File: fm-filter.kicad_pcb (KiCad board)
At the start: 2 copper layers, 57.2 x 29.2 mm, 7 parts, among them J1 SMA, J2 SMA

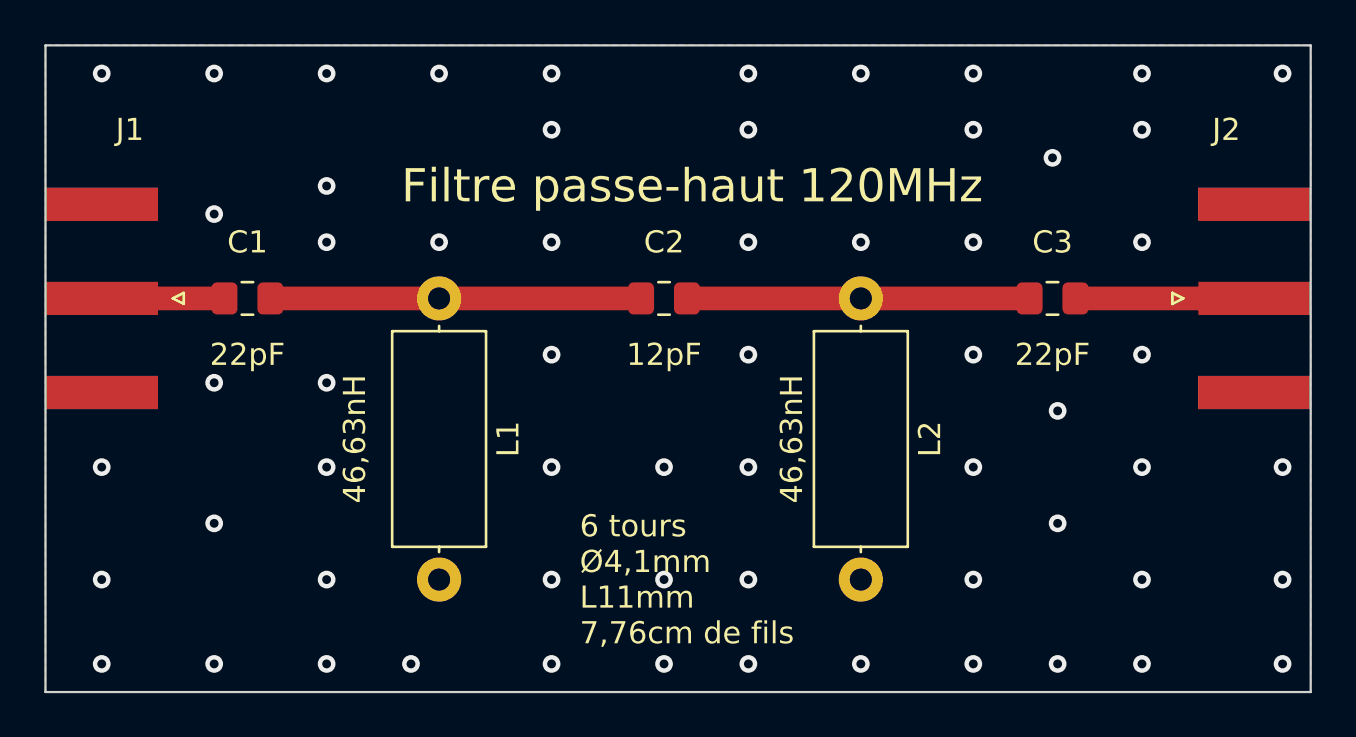
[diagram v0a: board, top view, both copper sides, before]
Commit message: feat: separative wall
Migrate to KiCAD v7.
Update README.md with initial manual and online order tentative.
Move to a newer version with mounting holes and pin holes for the wall
support.
Test integration with aisler.net
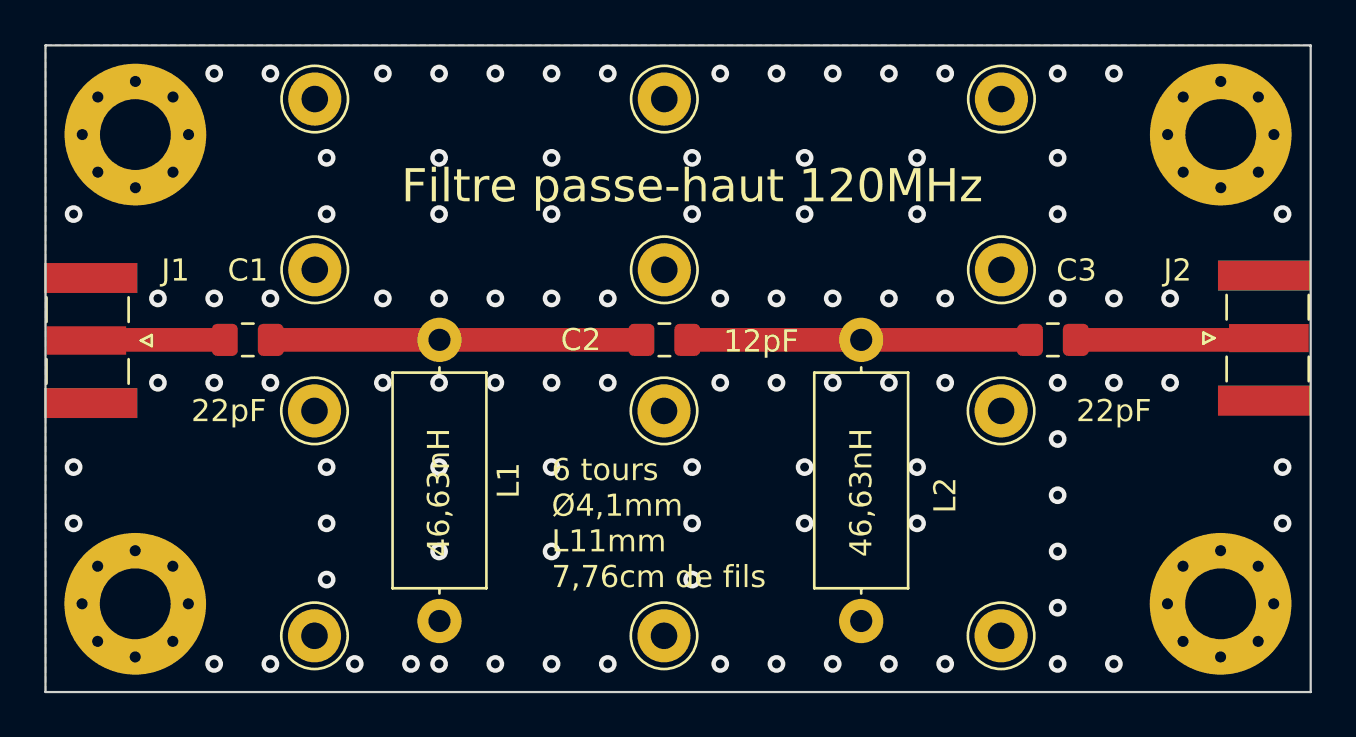
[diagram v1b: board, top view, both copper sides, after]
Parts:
- added MH1: Pin_D1.0mm_L10.0mm_LooseFit, Connector_Pin:Pin_D1.0mm_L10.0mm_LooseFit, F.Cu at (80.7, 34.2)
- added MH11: Pin_D1.0mm_L10.0mm_LooseFit, Connector_Pin:Pin_D1.0mm_L10.0mm_LooseFit, F.Cu at (96.5, 34.2)
- added MH12: Pin_D1.0mm_L10.0mm_LooseFit, Connector_Pin:Pin_D1.0mm_L10.0mm_LooseFit, F.Cu at (96.5, 41.9)
- added MH13: Pin_D1.0mm_L10.0mm_LooseFit, Connector_Pin:Pin_D1.0mm_L10.0mm_LooseFit, F.Cu at (96.5, 48.3)
- added MH14: Pin_D1.0mm_L10.0mm_LooseFit, Connector_Pin:Pin_D1.0mm_L10.0mm_LooseFit, F.Cu at (96.5, 58.4)
- added MH2: Pin_D1.0mm_L10.0mm_LooseFit, Connector_Pin:Pin_D1.0mm_L10.0mm_LooseFit, F.Cu at (80.7, 41.9)
- added MH21: Pin_D1.0mm_L10.0mm_LooseFit, Connector_Pin:Pin_D1.0mm_L10.0mm_LooseFit, F.Cu at (111.8, 34.2)
- added MH22: Pin_D1.0mm_L10.0mm_LooseFit, Connector_Pin:Pin_D1.0mm_L10.0mm_LooseFit, F.Cu at (111.8, 41.9)
- added MH23: Pin_D1.0mm_L10.0mm_LooseFit, Connector_Pin:Pin_D1.0mm_L10.0mm_LooseFit, F.Cu at (111.7, 48.3)
- added MH24: Pin_D1.0mm_L10.0mm_LooseFit, Connector_Pin:Pin_D1.0mm_L10.0mm_LooseFit, F.Cu at (111.7, 58.4)
- added MH3: Pin_D1.0mm_L10.0mm_LooseFit, Connector_Pin:Pin_D1.0mm_L10.0mm_LooseFit, F.Cu at (80.7, 48.3)
- added MH4: Pin_D1.0mm_L10.0mm_LooseFit, Connector_Pin:Pin_D1.0mm_L10.0mm_LooseFit, F.Cu at (80.7, 58.4)
- added MH_bottom_left: MountingHole_3.2mm_M3_Pad_Via, MountingHole:MountingHole_3.2mm_M3_Pad_Via, F.Cu at (72.6, 57.0)
- added MH_bottom_right: MountingHole_3.2mm_M3_Pad_Via, MountingHole:MountingHole_3.2mm_M3_Pad_Via, F.Cu at (121.7, 57.0)
- added MH_top_left: MountingHole_3.2mm_M3_Pad_Via, MountingHole:MountingHole_3.2mm_M3_Pad_Via, F.Cu at (72.6, 35.8)
- added MH_top_right: MountingHole_3.2mm_M3_Pad_Via, MountingHole:MountingHole_3.2mm_M3_Pad_Via, F.Cu at (121.7, 35.8)
- J1, J2: footprint Connector_Coaxial:SMA_Amphenol_132289_EdgeMount -> Connector_Coaxial:SMA_Samtec_SMA-J-P-X-ST-EM1_EdgeMount
- moved J1 1.97 mm to (70.6, 45.1), turned to -90 degrees
- moved C1 1.87 mm to (77.7, 45.1)
- moved C2 1.87 mm to (96.5, 45.1)
- moved C3 1.87 mm to (114.1, 45.1)
- moved L1 1.87 mm to (86.4, 45.1)
- moved L2 1.87 mm to (105.4, 45.1)
- moved J2 1.85 mm to (123.6, 45.0), turned to 90 degrees
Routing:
- net GND: track 0.00 -> 1.74 mm, vias 61 -> 99
- net Net-(J2-In): track 8.08 -> 8.98 mm
- net Net-(J1-In): track 5.55 -> 6.29 mm
